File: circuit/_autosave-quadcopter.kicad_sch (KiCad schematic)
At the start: 111 parts, among them J1 Conn_01x01_Female, J10 Conn_01x01_Female, J13 Conn_01x01_Female, J15 Conn_01x01_Female, J16 Conn_01x01_Female, J17 Conn_01x01_Female, J18 USB_C_Receptacle_USB2.0, J19 Conn_01x08_Male, J2 Conn_01x01_Female, J21 Conn_01x01_Female, J22 Conn_01x01_Female, J23 Conn_01x01_Female, J24 Conn_01x01_Female, J25 Conn_01x01_Female, J26 Conn_01x01_Female, J28 Conn_01x01_Female, J29 Conn_01x01_Female, J3 Conn_01x01_Female, J30 Conn_01x01_Female, J31 Conn_01x01_Female, J32 Conn_01x01_Female, J33 Conn_01x01_Female, J34 Conn_01x01_Female, J37 Conn_01x01_Female, J4 Conn_01x01_Female, J40 Conn_01x01_Female, J41 Conn_01x01_Female, J42 Conn_01x01_Female, J43 Conn_01x01_Female, J44 Conn_01x01_Female, J45 Conn_01x01_Female, J46 Conn_01x01_Female, J47 Conn_01x01_Female, J48 Conn_01x01_Female, J49 Conn_01x01_Female, J5 Conn_Coaxial, J50 Conn_01x01_Female, J6 Conn_01x06_Male, J7 Conn_01x01_Female, J8 Conn_01x01_Female, J9 Conn_01x01_Female, Q1 AO3400A, SW1 SW_DIP_x01, U1 STM32G431CBU6, U2 ICM-42605, U3 DPS310, U4 3V3, U5 5V out, 30V max, U6 2450FM07D0034T, U7 W25Q80DVUXIE TR (16M), U8 SX1281, Y1 16M, Y2 52Mhz, 12pF

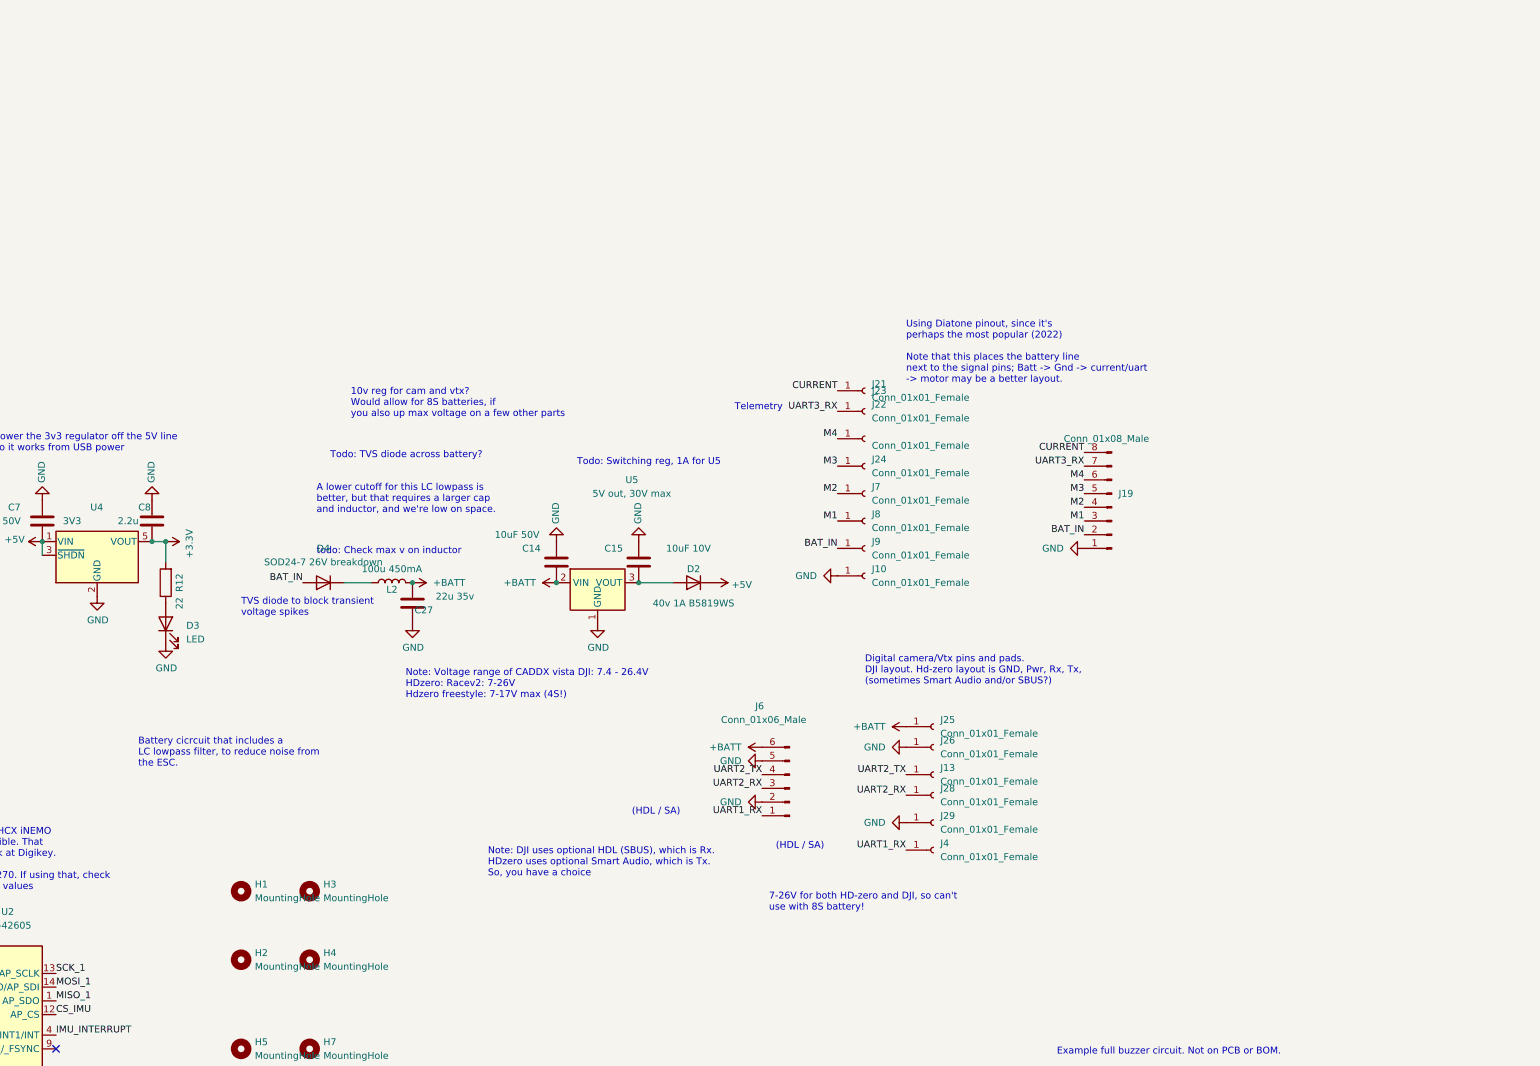
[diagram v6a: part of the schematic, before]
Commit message: Power section redid, including 10v reg added
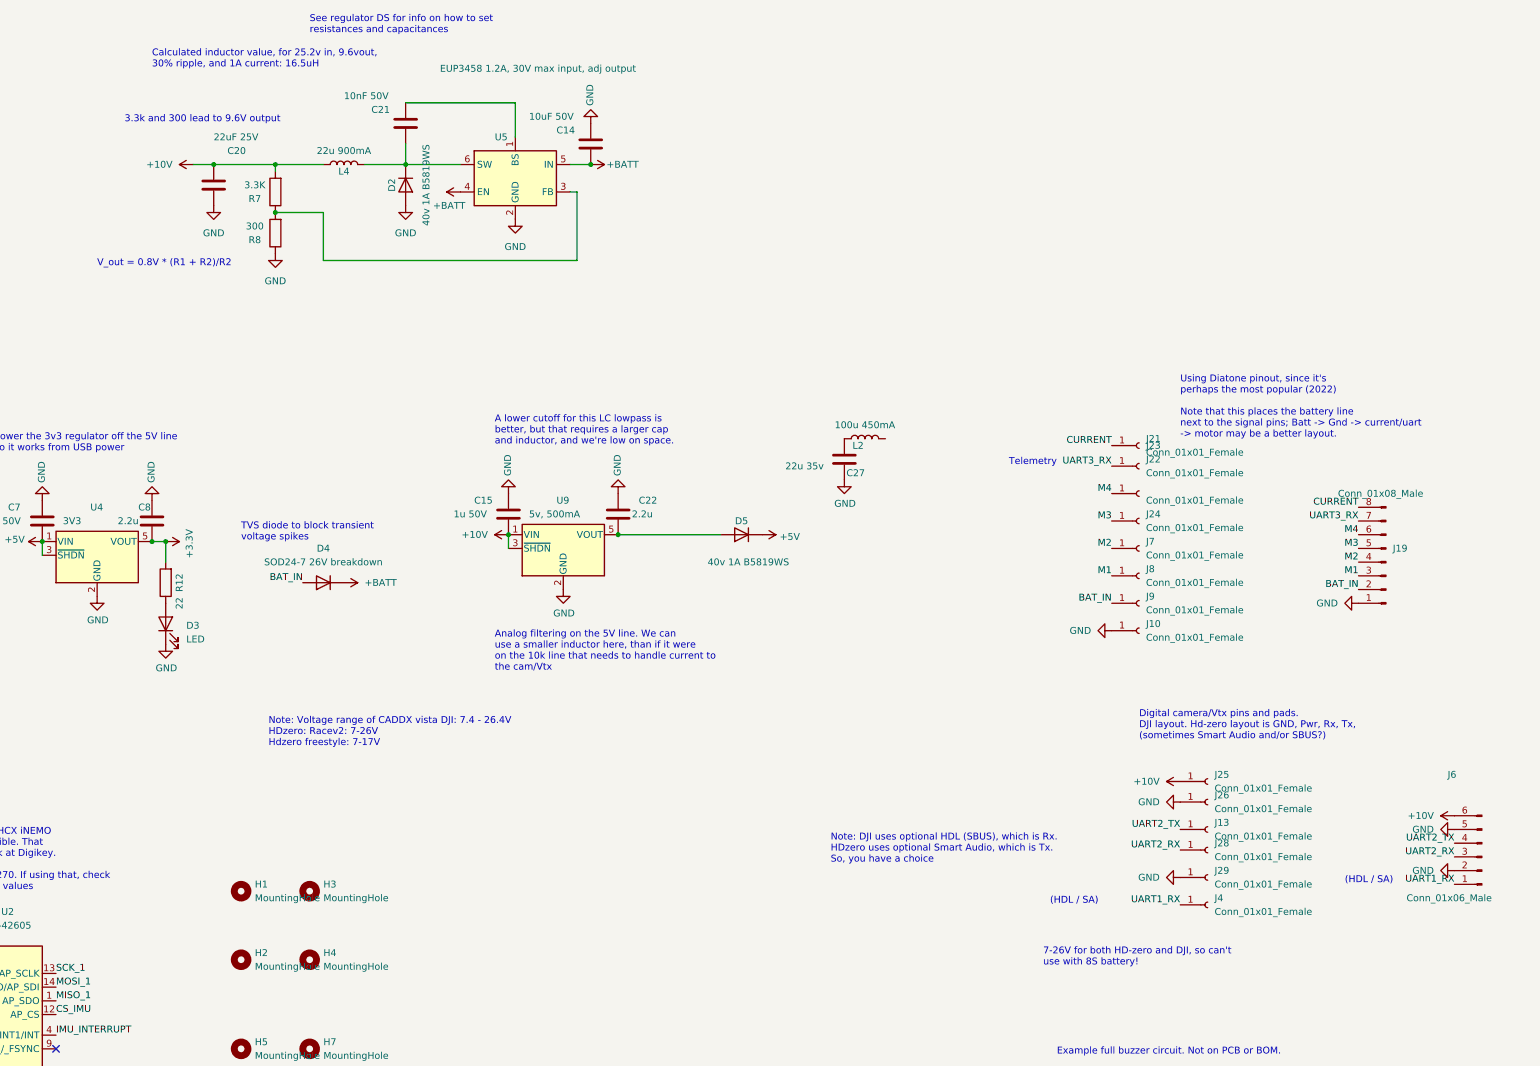
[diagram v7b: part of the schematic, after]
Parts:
- removed U5: 5V out, 30V max, Package_TO_SOT_SMD:SOT-89-3, symbol Regulator_Linear:HT75xx-1-SOT89
- added C20: 22uF 25V, Capacitor_SMD:C_0805_2012Metric, symbol Device:C
- added C21: 10nF 50V, Capacitor_SMD:C_0402_1005Metric, symbol Device:C
- added C22: 2.2u, Capacitor_SMD:C_0402_1005Metric, symbol Device:C
- added D5: 40v 1A B5819WS, Diode_SMD:D_SOD-323, symbol Device:D
- added L4: 22u 900mA, Anyleaf_Shared:SMNR4020 inductor, symbol Device:L
- added R7: 3.3K, Resistor_SMD:R_0402_1005Metric, symbol Device:R
- added R8: 300, Resistor_SMD:R_0402_1005Metric, symbol Device:R
- added U5: EUP3458 1.2A, 30V max input, adj output, Package_TO_SOT_SMD:TSOT-23-6, symbol Regulator_Switching:AAT1217ICA-1.2
- added U9: 5v, 500mA, Package_TO_SOT_SMD:TSOT-23-5, symbol water_monitor-rescue:MCP1802-3.3-Anyleaf_shared
- C15: value 10uF 10V -> 1u 50V; LCSC C19702 -> C15849
- C27, L2: now left out of the parts list
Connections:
- net +5V: now also D5.1 (K); no longer D2.1 (K)
- net +BATT: now also D4.1 (K), U5.4 (EN), U5.5 (IN); no longer C27.2, J25.1 (Pin_1), J6.6 (Pin_6), L2.2
- net GND: now also D2.2 (A), C20.2, C22.1, R8.1, U5.2 (GND), U9.2 (GND)
- net +10V: now reaches C15.2
- net +10V: now also J25.1 (Pin_1), J6.6 (Pin_6), C20.1, L4.1, R7.2, U9.1 (VIN), U9.3 (~{SHDN}); no longer D2.2 (A)
- net at L2.1: now also C27.2; no longer D4.1 (K)
- new net: C21.1, U5.1 (BS)
- new net: C21.2, D2.1 (K), L4.2, U5.6 (SW)
- new net: C22.2, D5.2 (A), U9.5 (VOUT)
- new net: R7.1, R8.2, U5.3 (FB)
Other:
- note added: "3.3k and 300 lead to 9.6V output"
- note added: "Analog filtering on the 5V line. We can use a smaller inductor here, than if it were on the 10k line that needs to handle current to the cam/Vtx"
- note added: "Calculated inductor value, for 25.2v in, 9.6vout, 30% ripple, and 1A current: 16.5uH"
- note added: "Note: Voltage range of CADDX vista DJI: 7.4 - 26.4V HDzero: Racev2: 7-26V Hdzero freestyle: 7-17V"
- note added: "See regulator DS for info on how to set resistances and capacitances"
- note added: "V_out = 0.8V * (R1 + R2)/R2"
- note removed: "10v reg for cam and vtx? Would allow for 8S batteries, if you also up max voltage on a few other parts"
- note removed: "Battery cicrcuit that includes a LC lowpass filter, to reduce noise from the ESC."
- note removed: "Note: Voltage range of CADDX vista DJI: 7.4 - 26.4V HDzero: Racev2: 7-26V Hdzero freestyle: 7-17V max (4S!)"
- note removed: "Todo: Switching reg, 1A for U5"
- note removed: "Todo: TVS diode across battery?"
- note removed: "todo: Check max v on inductor"
- moved on the sheet: C14, C27, D2, J10, J13, J19, J21, J22, J23, J24, J25, J26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

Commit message: Board is now routed!
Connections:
- net BUZZER_PWM: now also U1.9 (PA1); no longer U1.29 (PC6)
- net CS_FLASH: now also U1.29 (PC6); no longer U1.2 (PC13)
- net ELRS_DIO: now also U1.2 (PC13); no longer U1.9 (PA1)
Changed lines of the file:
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@@
     (effects (font (size 1.27 1.27)) (justify left bottom))
   )
-  (label "BUZZER_PWM" (at 143.51 114.3 0)
-    (effects (font (size 1.27 1.27)) (justify left bottom))
+  (label "BUZZER_PWM" (at 113.03 81.28 180)
+    (effects (font (size 1.27 1.27)) (justify right bottom))
   )
   (label "MOSI_3" (at 78.74 303.53 0)
@@
     (effects (font (size 1.27 1.27)) (justify right bottom))
   )
-  (label "CS_FLASH" (at 143.51 106.68 0)
+  (label "CS_FLASH" (at 143.51 114.3 0)
     (effects (font (size 1.27 1.27)) (justify left bottom))
   )
@@
     (effects (font (size 1.27 1.27)) (justify left bottom))
   )
-  (label "ELRS_DIO" (at 113.03 81.28 180)
-    (effects (font (size 1.27 1.27)) (justify right bottom))
+  (label "ELRS_DIO" (at 143.51 106.68 0)
+    (effects (font (size 1.27 1.27)) (justify left bottom))
   )
   (label "CS_ELRS" (at 109.22 64.77 180)
